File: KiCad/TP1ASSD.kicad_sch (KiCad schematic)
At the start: 67 parts, among them J1 Alimentacion, J10 JumperCtrlAS, J11 JumperCtrlSH, J2 GND, J3 Vi, J4 Jumper_FA, J5 Jumper_SH, J6 Jumper_AS, J7 Jumper_AS, J8 Vo, J9 GND(Vo), U1 TL082, U10 LM78xx, U11 LM79xx, U2 TL082, U3 TL082, U4 TL082, U5 LM311, U6 LM311, U7 LM311, U8 LF398_DIP8, U9 4016

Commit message: Agregue capas de desacople y DC zerooing para el SH
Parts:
- added C16, C17, C18, C19, C20, C21, C22, C23, C24, C25, C26, C27, C28, C29, C30, C31, C32, C33: 100n, TCLib:C_0805, symbol TCLib:C
- added R26: 33k, TCLib:R_0.25W, symbol TCLib:R
- added RV4: 1k, TCLib:RV_Preset_multivuelta_10mm_5mm, symbol TCLib:R_Potentiometer
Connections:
- net +10V: now also C16.1, C18.1, C20.1, C22.1, C25.2, C30.1, C32.1, RV4.1
- net +5V: now also C27.1, C29.1
- net -10V: now also C17.2, C19.2, C21.2, C23.2, C24.1, C31.1, C33.1, R26.2
- net -5V: now also C26.1, C28.1
- net GND: now also C16.2, C17.1, C18.2, C19.1, C20.2, C21.1, C22.2, C23.1, C24.2, C25.1, C26.2, C27.2, C28.2, C29.2, C30.2, C31.2, C32.2, C33.2
- net at U8.2 (Adj): now also RV4.2
- new net: R26.1, RV4.3

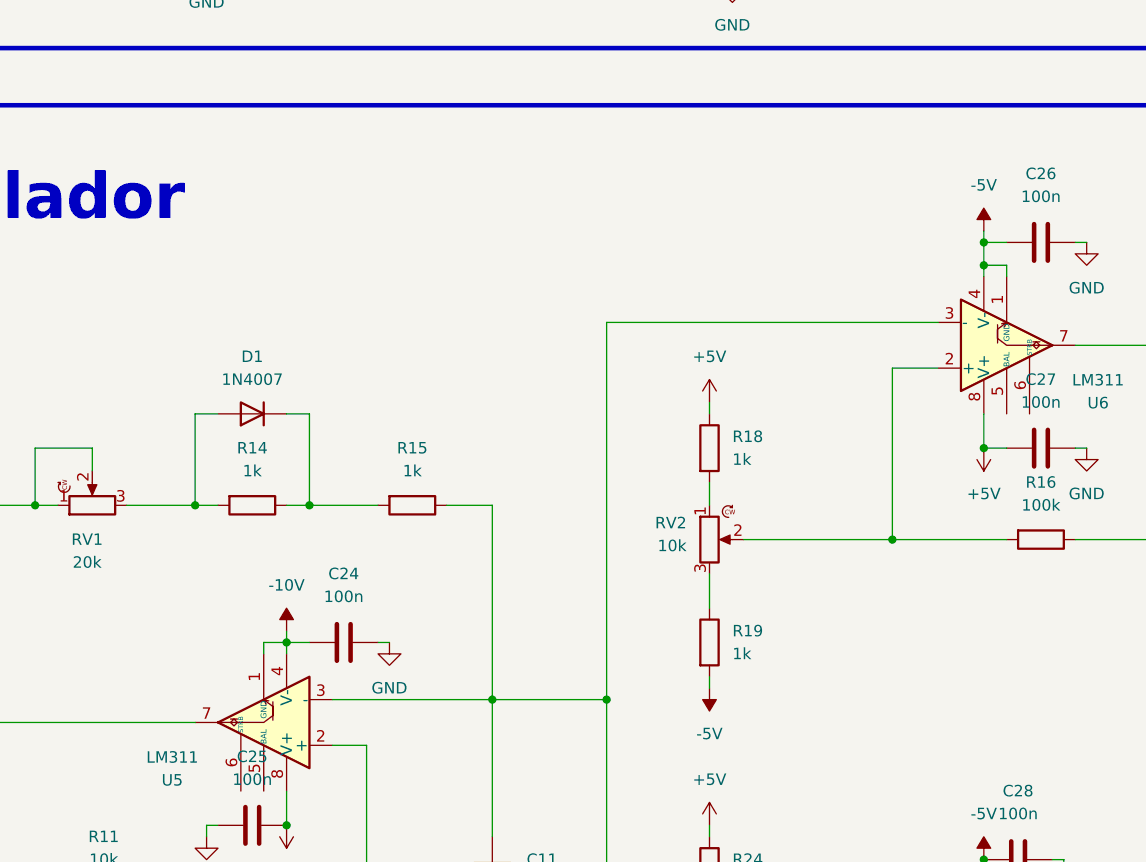
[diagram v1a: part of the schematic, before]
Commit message: Empece a rutear la alimentacion
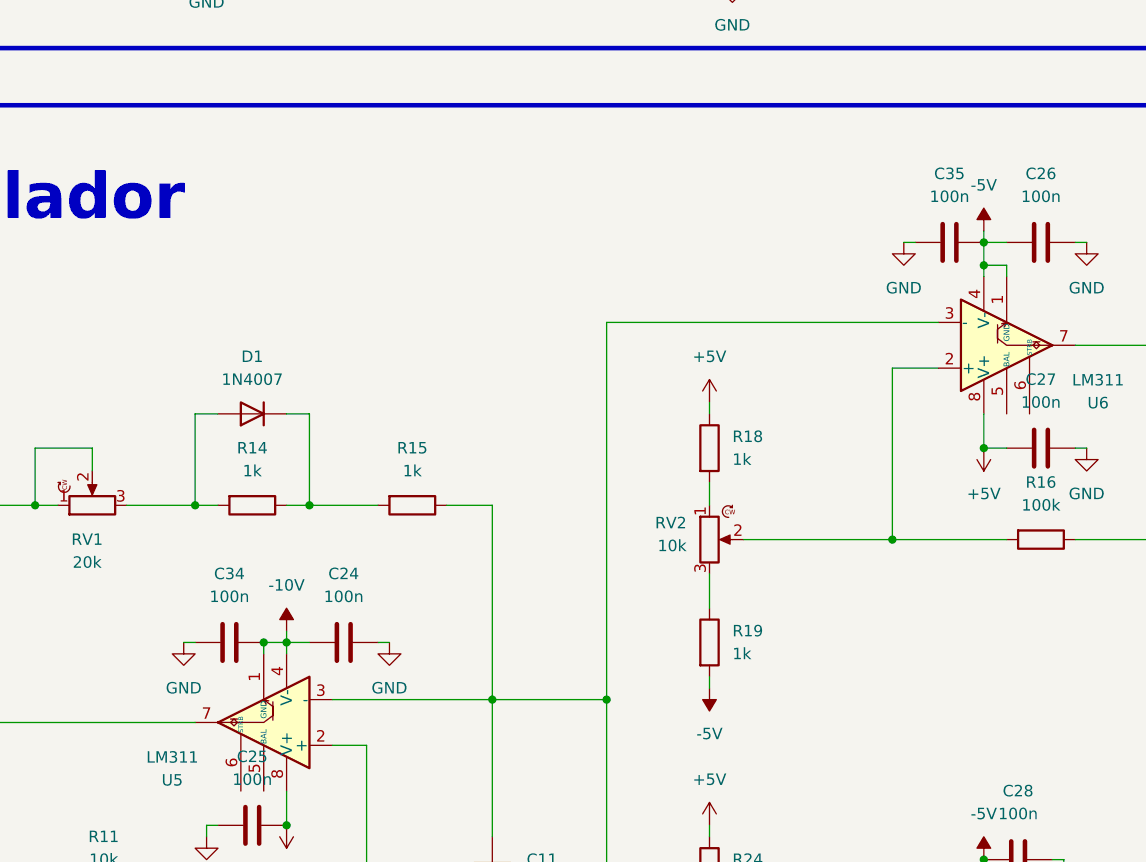
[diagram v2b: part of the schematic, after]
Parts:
- added C34: 100n, TCLib:C_5mm, symbol TCLib:C
- added C35: 100n, TCLib:C_0805, symbol TCLib:C
- C12, C13, C14, C15: footprint TCLib:C_5mm -> TCLib:C_0805
- C24, C25, C26, C27, C28, C29, C30: footprint TCLib:C_0805 -> TCLib:C_5mm
- C32: footprint TCLib:C_0805 -> TCLib:C_2.5mm
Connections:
- net -10V: now also C34.1
- net -5V: now also C35.1
- net GND: now also C34.2, C35.2

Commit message: Termine alimentacion
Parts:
- C16, C17, C18, C19, C20, C21, C22, C23, C31, C33: footprint TCLib:C_0805 -> TCLib:C_5mm
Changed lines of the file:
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@@
 			)
 		)
-		(property "Footprint" "TCLib:C_0805"
+		(property "Footprint" "TCLib:C_5mm"
 			(at 58.42 30.988 0)
 			(effects
@@
 			)
 		)
-		(property "Footprint" "TCLib:C_0805"
+		(property "Footprint" "TCLib:C_5mm"
 			(at 27.94 23.368 0)
 			(effects
@@
 			)
 		)
-		(property "Footprint" "TCLib:C_0805"
+		(property "Footprint" "TCLib:C_5mm"
 			(at 27.94 30.988 0)
 			(effects
@@
 			)
 		)
-		(property "Footprint" "TCLib:C_0805"
+		(property "Footprint" "TCLib:C_5mm"
 			(at 58.42 23.368 0)
 			(effects
@@
 			)
 		)
-		(property "Footprint" "TCLib:C_0805"
+		(property "Footprint" "TCLib:C_5mm"
 			(at 54.61 90.678 0)
 			(effects
@@
 			)
 		)
-		(property "Footprint" "TCLib:C_0805"
+		(property "Footprint" "TCLib:C_5mm"
 			(at 54.61 98.298 0)
 			(effects
@@
 			)
 		)
-		(property "Footprint" "TCLib:C_0805"
+		(property "Footprint" "TCLib:C_5mm"
 			(at 60.96 98.298 0)
 			(effects
@@
 			)
 		)
-		(property "Footprint" "TCLib:C_0805"
+		(property "Footprint" "TCLib:C_5mm"
 			(at 60.96 90.678 0)
 			(effects
@@
 			)
 		)
-		(property "Footprint" "TCLib:C_0805"
+		(property "Footprint" "TCLib:C_5mm"
 			(at 270.002 81.28 0)
 			(effects
@@
 			)
 		)
-		(property "Footprint" "TCLib:C_0805"
+		(property "Footprint" "TCLib:C_5mm"
 			(at 294.132 146.05 0)
 			(effects
